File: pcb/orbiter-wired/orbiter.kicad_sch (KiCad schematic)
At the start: 26 parts, among them U1 TPS82140

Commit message: Latest schematic
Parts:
- U1: LCSC Part # (none) -> C544385
- USB_U1: LCSC Part # C7519 -> C323793
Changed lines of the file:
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@@
+			)
+		)
+		(property "LCSC Part #" "C544385"
+			(at 72.39 167.64 0)
+			(effects
+				(font
+					(size 1.27 1.27)
+				)
+				(hide yes)
 			)
 		)
@@
 			)
 		)
-		(property "LCSC Part #" "C7519"
+		(property "LCSC Part #" "C323793"
 			(at 144.78 170.18 0)
 			(effects

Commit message: Orbiter wired v1.0 gerber & cleanup of old project files
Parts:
- 3V3_TP1, BOOT0_TP1, H1, H2, H3, H4, H5, H6, H7, NRST_TP1, SWCLK_TP1, SWDIO_TP1, USART_TP1, USB_CONN_DN_TP1, USB_CONN_DP_TP1, USB_DN_TP1, USB_DP_TP1, VBUS_TP1: JLCPCB Part # N/A -> (none)
- U1: JLCPCB Part # C544385 -> (none); LCSC Part # C544385 -> (none)
- USB_U1: JLCPCB Part # C323793 -> (none); LCSC Part # C323793 -> (none)

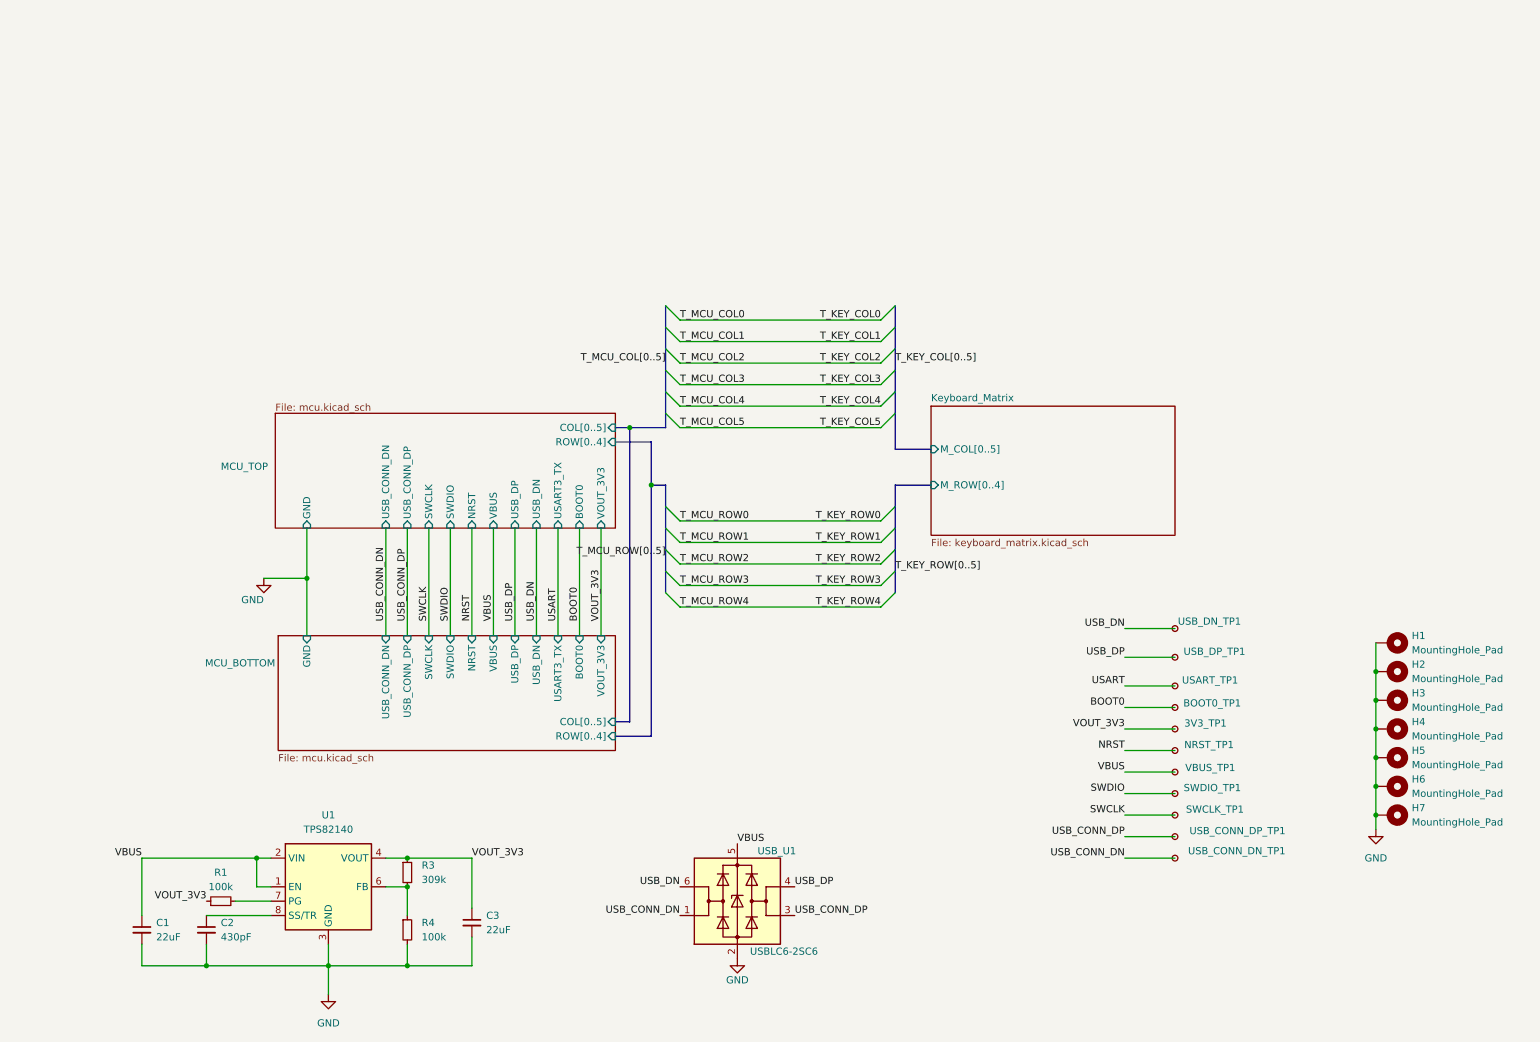
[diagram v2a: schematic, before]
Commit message: Move symbols into their own folder
Add footprint and symbol for TPS82140SILR that is correct size
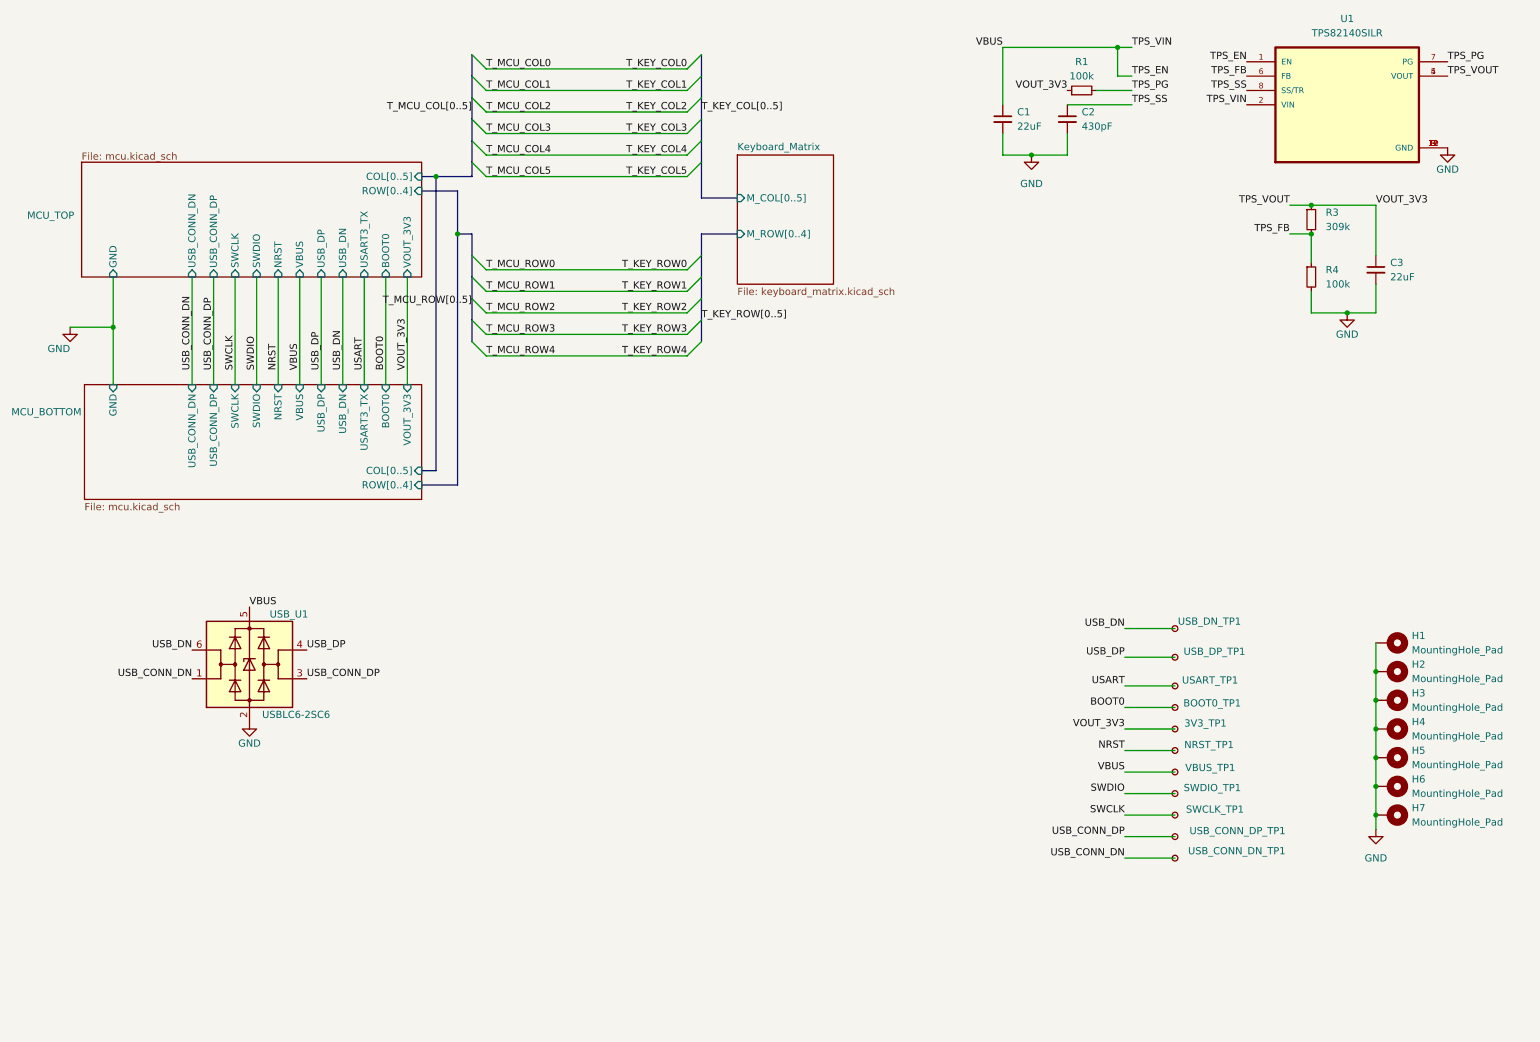
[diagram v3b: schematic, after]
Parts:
- removed U1: TPS82140, Package_LGA:Texas_SIL0008D_MicroSiP-8-1EP_2.8x3mm_P0.65mm_EP1.1x1.9mm, symbol Regulator_Switching:TPS82140
- added U1: TPS82140SILR, TPS82140SILR:TPS82140SILR, symbol TPS82140SILR:TPS82140SILR
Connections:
- net GND: now also U1.10 (GND), U1.11 (GND), U1.12 (GND), U1.3 (GND), U1.9 (GND)
- net TPS_FB: now reaches R3.2, R4.1
- net TPS_FB: now also U1.6 (FB)
- net TPS_PG: now reaches R1.2
- net TPS_PG: now also U1.7 (PG)
- net TPS_SS: now reaches C2.1
- net TPS_SS: now also U1.8 (SS/TR)
- net VBUS renamed TPS_EN
- net TPS_EN: now also U1.1 (EN), U1.2 (VIN)
- net VOUT_3V3 renamed TPS_VOUT
- net TPS_VOUT: now also U1.4 (VOUT), U1.5 (VOUT)
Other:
- moved on the sheet: C1, C2, C3, R1, R3, R4, USB_U1
